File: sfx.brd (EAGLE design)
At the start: 58 x 28.1 mm, 19 parts, among them IC1 74LS00N, IC2 74LS04N, IC4 YM3812, IC5 YM3014B, IC6 TL072P

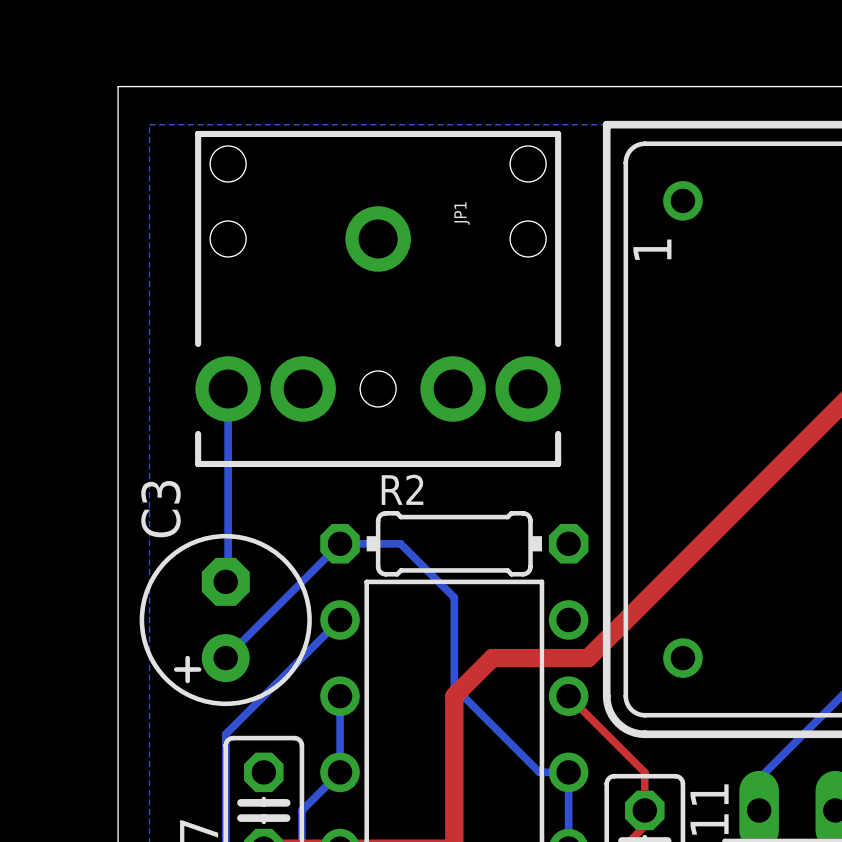
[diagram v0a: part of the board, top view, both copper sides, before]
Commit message: moved the audio jack
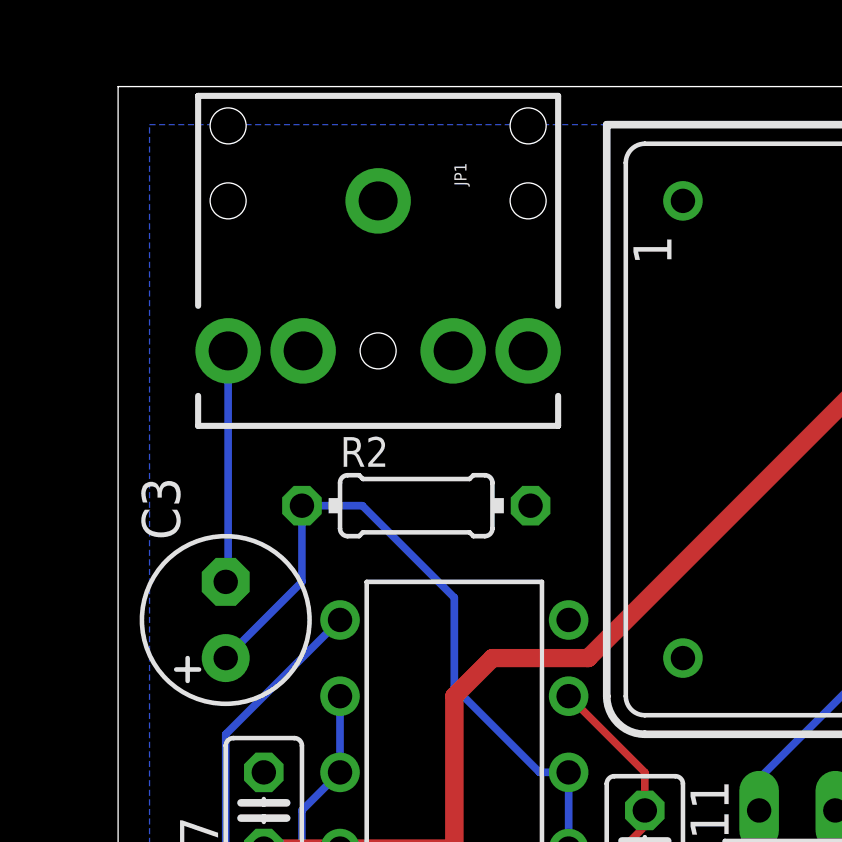
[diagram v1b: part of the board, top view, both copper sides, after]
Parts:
- moved R2 1.80 mm to (-102.9, -24.1)
- moved JP1 1.27 mm to (-104.1, -14.0)
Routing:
- net N$14: track 20.5 -> 23.0 mm
- net N$12: track 6.51 -> 7.78 mm
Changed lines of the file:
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@@
 <element name="IC5" library="ic-package" package="DIL08" value="YM3014B" x="-99.06" y="-43.18" rot="R90"/>
 <element name="C1" library="rcl" package="E2,5-6" value="10u" x="-107.95" y="-48.26" rot="R90"/>
-<element name="R2" library="rcl" package="0204/7" value="10k" x="-101.6" y="-25.4"/>
+<element name="R2" library="rcl" package="0204/7" value="10k" x="-102.87" y="-24.13"/>
 <element name="C3" library="rcl" package="E2,5-6" value="10u" x="-109.22" y="-27.94" rot="R90"/>
 <element name="C4" library="rcl" package="E2,5-6" value="10u" x="-109.22" y="-40.64" rot="R180"/>
@@
 <element name="C8" library="rcl" package="C025-025X050" value="100n" x="-95.25" y="-50.8"/>
 <element name="C9" library="rcl" package="C025-025X050" value="100n" x="-81.28" y="-13.97" rot="R270"/>
-<element name="JP1" library="SparkFun-Connectors" package="AUDIO-JACK" value="" x="-104.14" y="-15.24" rot="R270"/>
+<element name="JP1" library="SparkFun-Connectors" package="AUDIO-JACK" value="" x="-104.14" y="-13.97" rot="R270"/>
 </elements>
 <signals>
@@
 <wire x1="-98.76019375" y1="-33.02" x2="-101.6" y2="-30.18019375" width="0.254" layer="16"/>
 <wire x1="-101.6" y1="-30.18019375" x2="-101.6" y2="-27.19605" width="0.254" layer="16"/>
-<wire x1="-101.6" y1="-27.19605" x2="-103.39605" y2="-25.4" width="0.254" layer="16"/>
-<wire x1="-103.39605" y1="-25.4" x2="-105.41" y2="-25.4" width="0.254" layer="16"/>
-<wire x1="-105.41" y1="-25.4" x2="-109.22" y2="-29.21" width="0.254" layer="16"/>
+<wire x1="-101.6" y1="-27.19605" x2="-104.66605" y2="-24.13" width="0.254" layer="16"/>
+<wire x1="-104.66605" y1="-24.13" x2="-106.68" y2="-24.13" width="0.254" layer="16"/>
+<wire x1="-106.68" y1="-24.13" x2="-106.68" y2="-26.67" width="0.254" layer="16"/>
+<wire x1="-106.68" y1="-26.67" x2="-109.22" y2="-29.21" width="0.254" layer="16"/>
 </signal>
 <signal name="D1">
@@
 <contactref element="JP1" pad="TIP"/>
 <wire x1="-109.22" y1="-26.67" x2="-109.14" y2="-26.67" width="0.254" layer="16"/>
-<wire x1="-109.14" y1="-26.67" x2="-109.14" y2="-20.24" width="0.254" layer="16"/>
+<wire x1="-109.14" y1="-26.67" x2="-109.14" y2="-18.97" width="0.254" layer="16"/>
 </signal>
 <signal name="N$10">
